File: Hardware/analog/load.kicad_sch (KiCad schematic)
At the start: 21 parts, among them J201 Würth 74651194R, J202 Würth 74651194R, Q201 IXTH80N075L2, U202 LM431SC

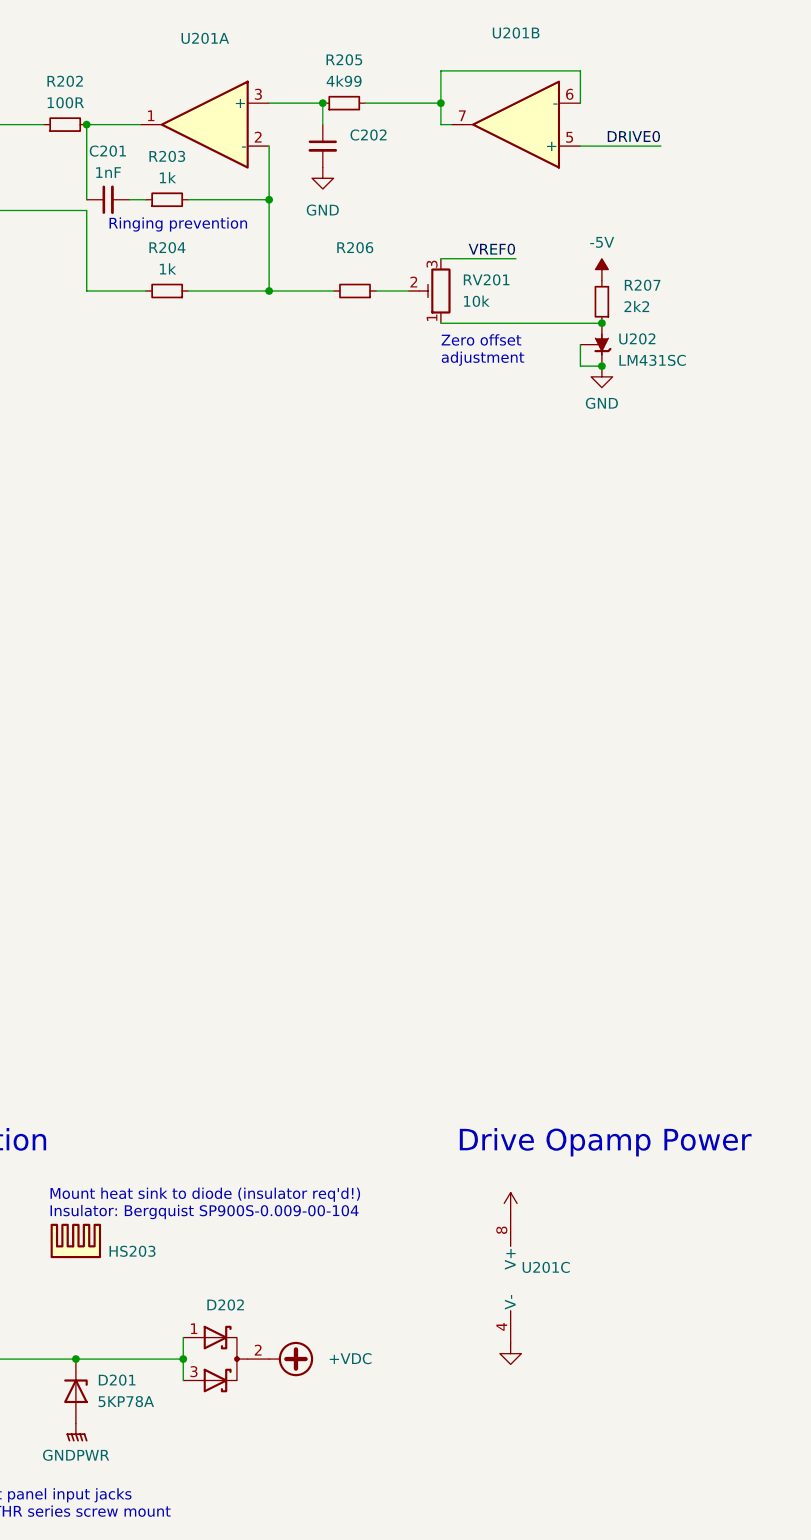
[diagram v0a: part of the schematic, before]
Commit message: Minor analog board layout tweaks
- Mostly to do with the last of the analog bits for the first channel
  (reisstors and capacitors, as well as the zero offset trimmer)
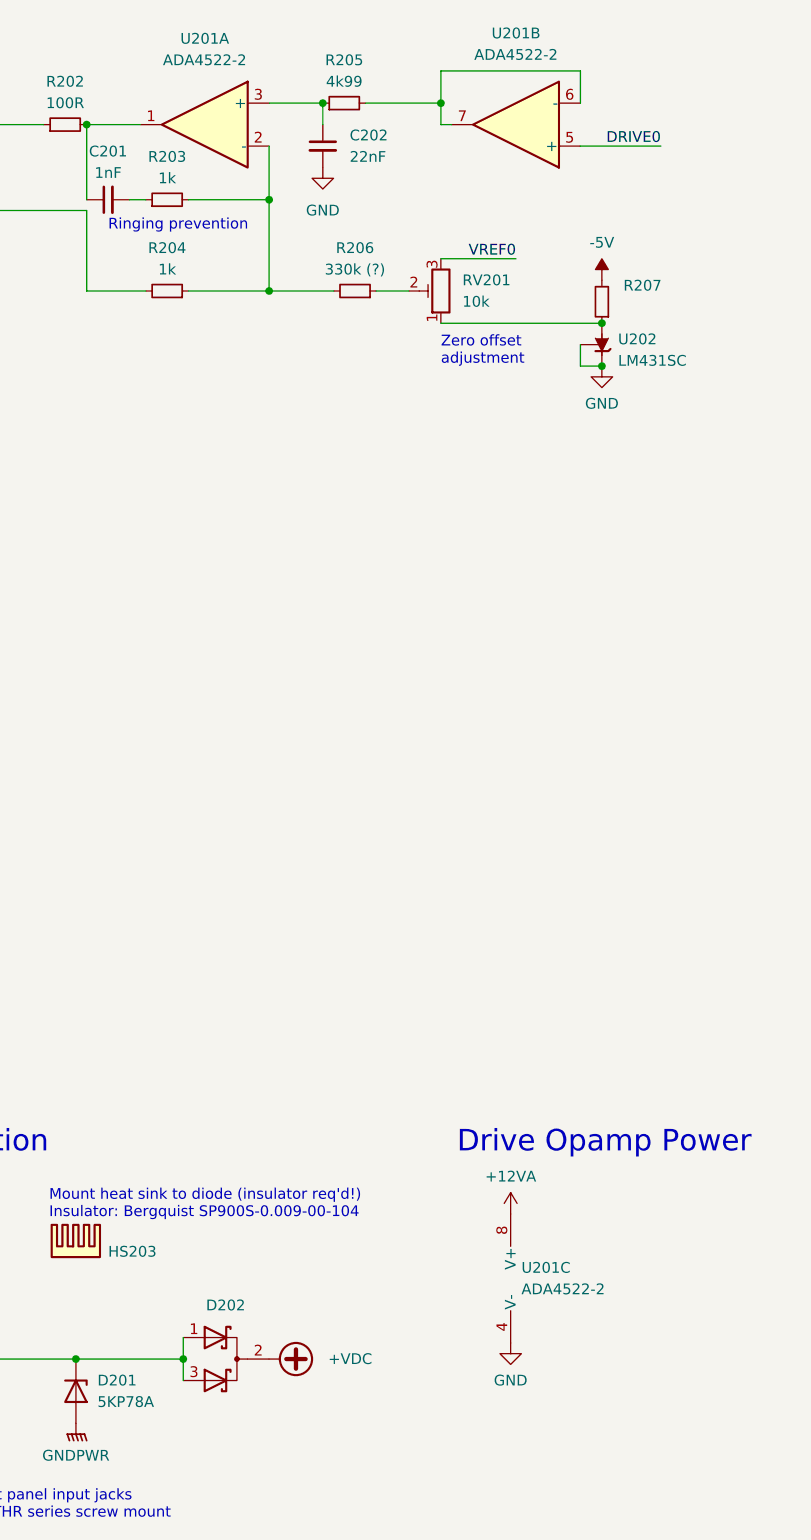
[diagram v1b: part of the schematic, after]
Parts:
- C202: value (none) -> 22nF; footprint (none) -> Capacitor_SMD:C_0805_2012Metric_Pad1.18x1.45mm_HandSolder
- R206: value (none) -> 330k (?)
- R207: value 2k2 -> (none); footprint Resistor_SMD:R_0805_2012Metric_Pad1.20x1.40mm_HandSolder -> (none); MPN RMC1/10-222JTP -> CR0805-JW-102ELF
- U201: value (none) -> ADA4522-2; footprint (none) -> Package_SO:SOIC-8_3.9x4.9mm_P1.27mm
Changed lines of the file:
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@@
       (effects (font (size 1.27 1.27)) (justify left))
     )
-    (property "Value" "" (id 1) (at 82.55 34.2962 0)
-      (effects (font (size 1.27 1.27)) (justify left))
-    )
-    (property "Footprint" "" (id 2) (at 79.375 33.02 0)
+    (property "Value" "22nF" (id 1) (at 82.55 34.2962 0)
+      (effects (font (size 1.27 1.27)) (justify left))
+    )
+    (property "Footprint" "Capacitor_SMD:C_0805_2012Metric_Pad1.18x1.45mm_HandSolder" (id 2) (at 79.375 33.02 0)
       (effects (font (size 1.27 1.27)) hide)
     )
@@
       (effects (font (size 1.27 1.27)) hide)
     )
-    (property "Value" "" (id 1) (at 101.6 154.94 0))
+    (property "Value" "+12VA" (id 1) (at 101.6 154.94 0))
     (property "Footprint" "" (id 2) (at 101.6 159.385 0)
       (effects (font (size 1.27 1.27)) hide)
@@
     (in_bom yes) (on_board yes) (fields_autoplaced)
     (property "Reference" "U201" (id 0) (at 65.405 20.32 0))
-    (property "Value" "" (id 1) (at 65.405 22.86 0))
-    (property "Footprint" "" (id 2) (at 65.405 30.48 0)
+    (property "Value" "ADA4522-2" (id 1) (at 65.405 22.86 0))
+    (property "Footprint" "Package_SO:SOIC-8_3.9x4.9mm_P1.27mm" (id 2) (at 65.405 30.48 0)
       (effects (font (size 1.27 1.27)) hide)
     )
@@
       (effects (font (size 1.27 1.27)) (justify right))
     )
-    (property "Value" "" (id 1) (at 102.87 168.2749 0)
-      (effects (font (size 1.27 1.27)) (justify right))
-    )
-    (property "Footprint" "" (id 2) (at 99.06 167.005 0)
+    (property "Value" "ADA4522-2" (id 1) (at 102.87 168.2749 0)
+      (effects (font (size 1.27 1.27)) (justify right))
+    )
+    (property "Footprint" "Package_SO:SOIC-8_3.9x4.9mm_P1.27mm" (id 2) (at 99.06 167.005 0)
       (effects (font (size 1.27 1.27)) hide)
     )
@@
       (effects (font (size 1.27 1.27)) (justify right))
     )
-    (property "Value" "2k2" (id 1) (at 114.935 52.07 0)
-      (effects (font (size 1.27 1.27)) (justify right))
-    )
-    (property "Footprint" "Resistor_SMD:R_0805_2012Metric_Pad1.20x1.40mm_HandSolder" (id 2) (at 112.395 51.435 0)
+    (property "Value" "" (id 1) (at 114.935 52.07 0)
+      (effects (font (size 1.27 1.27)) (justify right))
+    )
+    (property "Footprint" "" (id 2) (at 112.395 51.435 0)
       (effects (font (size 1.27 1.27)) hide)
     )
@@
       (effects (font (size 1.27 1.27)) hide)
     )
-    (property "MPN" "RMC1/10-222JTP" (id 4) (at 112.395 51.435 0)
+    (property "MPN" "CR0805-JW-102ELF" (id 4) (at 112.395 51.435 0)
       (effects (font (size 1.27 1.27)) hide)
     )
@@
     (in_bom yes) (on_board yes) (fields_autoplaced)
     (property "Reference" "U201" (id 0) (at 102.235 19.685 0))
-    (property "Value" "" (id 1) (at 102.235 22.225 0))
-    (property "Footprint" "" (id 2) (at 102.235 30.48 0)
+    (property "Value" "ADA4522-2" (id 1) (at 102.235 22.225 0))
+    (property "Footprint" "Package_SO:SOIC-8_3.9x4.9mm_P1.27mm" (id 2) (at 102.235 30.48 0)
       (effects (font (size 1.27 1.27)) hide)
     )
@@
       (effects (font (size 1.27 1.27)) hide)
     )
-    (property "Value" "" (id 1) (at 101.6 179.07 0))
+    (property "Value" "GND" (id 1) (at 101.6 179.07 0))
     (property "Footprint" "" (id 2) (at 101.6 174.625 0)
       (effects (font (size 1.27 1.27)) hide)
@@
     (in_bom yes) (on_board yes)
     (property "Reference" "R206" (id 0) (at 83.185 45.085 90))
-    (property "Value" "" (id 1) (at 83.185 47.625 90))
+    (property "Value" "330k (?)" (id 1) (at 83.185 47.625 90))
     (property "Footprint" "Resistor_SMD:R_0805_2012Metric_Pad1.20x1.40mm_HandSolder" (id 2) (at 83.185 50.165 0)
       (effects (font (size 1.27 1.27)) hide)

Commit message: More tweaks to load board
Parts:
- R207: value (none) -> 1k; footprint (none) -> Resistor_SMD:R_0805_2012Metric_Pad1.20x1.40mm_HandSolder
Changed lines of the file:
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@@
   (symbol (lib_id "power:+12VA") (at 101.6 159.385 0) (unit 1)
     (in_bom yes) (on_board yes)
-    (property "Reference" "#PWR?" (id 0) (at 101.6 163.195 0)
+    (property "Reference" "#PWR0208" (id 0) (at 101.6 163.195 0)
       (effects (font (size 1.27 1.27)) hide)
     )
@@
       (effects (font (size 1.27 1.27)) (justify right))
     )
-    (property "Value" "" (id 1) (at 114.935 52.07 0)
-      (effects (font (size 1.27 1.27)) (justify right))
-    )
-    (property "Footprint" "" (id 2) (at 112.395 51.435 0)
+    (property "Value" "1k" (id 1) (at 114.935 52.07 0)
+      (effects (font (size 1.27 1.27)) (justify right))
+    )
+    (property "Footprint" "Resistor_SMD:R_0805_2012Metric_Pad1.20x1.40mm_HandSolder" (id 2) (at 112.395 51.435 0)
       (effects (font (size 1.27 1.27)) hide)
     )
@@
   (symbol (lib_id "power:GND") (at 101.6 174.625 0) (unit 1)
     (in_bom yes) (on_board yes) (fields_autoplaced)
-    (property "Reference" "#PWR?" (id 0) (at 101.6 180.975 0)
-      (effects (font (size 1.27 1.27)) hide)
-    )
+    (property "Reference" "#PWR0209" (id 0) (at 101.6 180.975 0)
+      (effects (font (size 1.27 1.27)) hide)
+    )

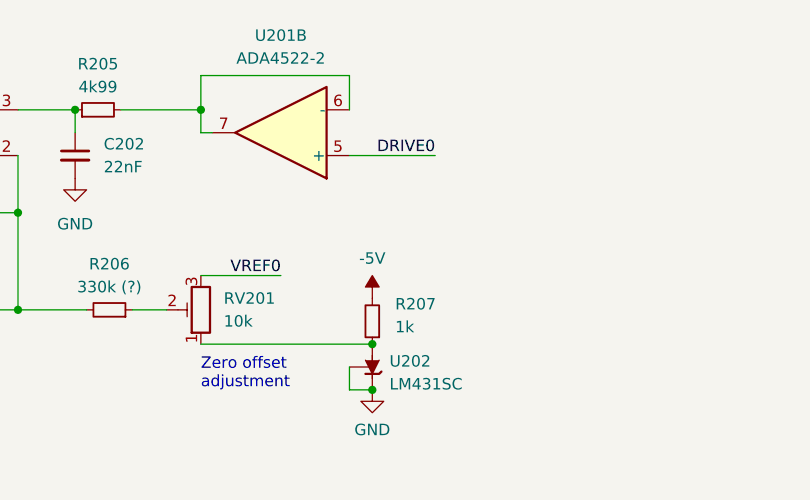
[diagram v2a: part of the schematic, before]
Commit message: Add ADC aliasing filters
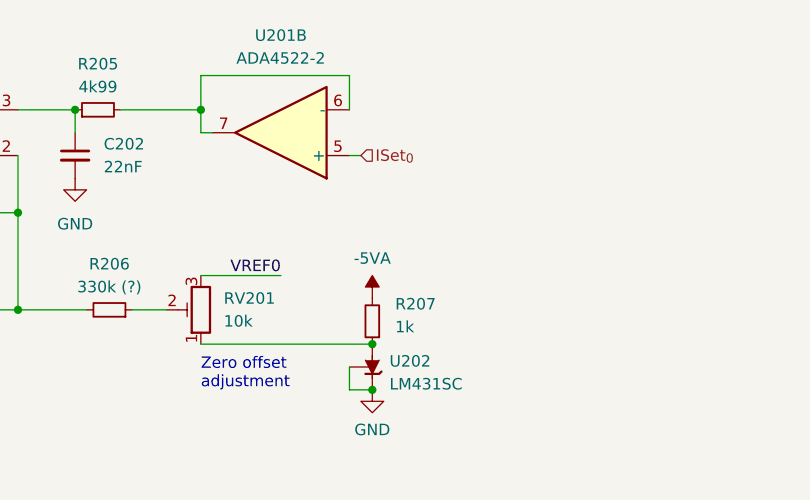
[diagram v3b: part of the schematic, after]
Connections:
- net -5V renamed -5VA
- net DRIVE0 renamed ISet_{0}
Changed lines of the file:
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@@
+    (stroke (width 0) (type default) (color 0 0 0 0))
+  )
+  (wire (pts (xy 109.855 33.02) (xy 111.125 33.02))
     (stroke (width 0) (type default) (color 0 0 0 0))
   )
@@
   )
   (wire (pts (xy 40.005 30.48) (xy 46.355 30.48))
-    (stroke (width 0) (type default) (color 0 0 0 0))
-  )
-  (wire (pts (xy 109.855 33.02) (xy 119.38 33.02))
     (stroke (width 0) (type default) (color 0 0 0 0))
   )
@@
     (effects (font (size 1.27 1.27)) (justify left bottom))
   )
-  (label "DRIVE0" (at 119.38 33.02 180)
-    (effects (font (size 1.27 1.27)) (justify right bottom))
-  )
   (label "VBUS_IN" (at 31.75 176.53 0)
     (effects (font (size 1.27 1.27)) (justify left bottom))
@@
   (label "VREF0" (at 102.235 46.355 180)
     (effects (font (size 1.27 1.27)) (justify right bottom))
+  )
+  (hierarchical_label "ISet_{0}" (shape input) (at 111.125 33.02 0)
+    (effects (font (size 1.27 1.27)) (justify left))
   )
   (symbol (lib_id "Device:R_Small") (at 60.96 39.37 90) (unit 1)
@@
     (pin "8")
   )
-  (symbol (lib_id "power:-5V") (at 112.395 48.895 0) (mirror y) (unit 1)
-    (in_bom yes) (on_board yes)
-    (property "Reference" "#PWR0206" (id 0) (at 112.395 46.355 0)
-      (effects (font (size 1.27 1.27)) hide)
-    )
-    (property "Value" "-5V" (id 1) (at 112.395 44.45 0))
-    (property "Footprint" "" (id 2) (at 112.395 48.895 0)
-      (effects (font (size 1.27 1.27)) hide)
-    )
-    (property "Datasheet" "" (id 3) (at 112.395 48.895 0)
-      (effects (font (size 1.27 1.27)) hide)
-    )
-    (pin "1")
-  )
   (symbol (lib_id "power:+VDC") (at 73.025 176.53 270) (unit 1)
     (in_bom yes) (on_board yes) (fields_autoplaced)
@@
       (effects (font (size 1.27 1.27)) hide)
     )
+    (pin "1")
+  )
+  (symbol (lib_id "power:-5VA") (at 112.395 48.895 0) (unit 1)
+    (in_bom yes) (on_board yes)
+    (property "Reference" "#PWR0118" (id 0) (at 112.395 46.355 0)
+      (effects (font (size 1.27 1.27)) hide)
+    )
+    (property "Value" "-5VA" (id 1) (at 112.395 44.45 0))
+    (property "Footprint" "" (id 2) (at 112.395 48.895 0)
+      (effects (font (size 1.27 1.27)) hide)
+    )
+    (property "Datasheet" "" (id 3) (at 112.395 48.895 0)
+      (effects (font (size 1.27 1.27)) hide)
+    )

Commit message: More tweaks to analog board
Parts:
- removed HS202: 2x C40-058-AE, programmable-load:C40-058-AE-DUAL, symbol Mechanical:Heatsink
- added U203: (no value), Package_TO_SOT_THT:TO-92_Inline_Wide, symbol programmable-load:LMT86LPM
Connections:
- net GND: now also U203.3 (GND)
- new net +3V3: U203.1 (Vdd)
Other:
- note added: "Temp Sensing"
- moved on the sheet: HS201
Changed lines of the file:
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@@
     (stroke (width 0) (type default) (color 0 0 0 0))
+  )
+  (text "Temp Sensing" (at 19.05 123.19 0)
+    (effects (font (size 2.54 2.54)) (justify left bottom))
   )
   (text "Drive Opamp Power" (at 95.25 152.4 0)
@@
     (pin "1")
   )
-  (symbol (lib_id "Mechanical:Heatsink") (at 177.165 156.21 270) (unit 1)
-    (in_bom yes) (on_board yes)
-    (property "Reference" "HS202" (id 0) (at 181.61 154.94 90)
-      (effects (font (size 1.27 1.27)) (justify left))
-    )
-    (property "Value" "2x C40-058-AE" (id 1) (at 181.61 157.48 90)
-      (effects (font (size 1.27 1.27)) (justify left))
-    )
-    (property "Footprint" "programmable-load:C40-058-AE-DUAL" (id 2) (at 177.165 156.5148 0)
-      (effects (font (size 1.27 1.27)) hide)
-    )
-    (property "Datasheet" "~" (id 3) (at 177.165 156.5148 0)
-      (effects (font (size 1.27 1.27)) hide)
-    )
-    (property "MPN" "C40-058-AE" (id 4) (at 177.165 156.21 90)
-      (effects (font (size 1.27 1.27)) hide)
-    )
+  (symbol (lib_id "power:+3V3") (at 33.02 125.73 270) (unit 1)
+    (in_bom yes) (on_board yes)
+    (property "Reference" "#PWR0206" (id 0) (at 29.21 125.73 0)
+      (effects (font (size 1.27 1.27)) hide)
+    )
+    (property "Value" "" (id 1) (at 36.195 125.73 90)
+      (effects (font (size 1.27 1.27)) (justify left))
+    )
+    (property "Footprint" "" (id 2) (at 33.02 125.73 0)
+      (effects (font (size 1.27 1.27)) hide)
+    )
+    (property "Datasheet" "" (id 3) (at 33.02 125.73 0)
+      (effects (font (size 1.27 1.27)) hide)
+    )
+    (pin "1")
   )
   (symbol (lib_id "Connector:Screw_Terminal_01x01") (at 26.67 182.88 180) (unit 1)
@@
     (pin "2")
   )
-  (symbol (lib_id "Mechanical:Heatsink") (at 177.165 148.59 270) (unit 1)
-    (in_bom yes) (on_board yes)
-    (property "Reference" "HS201" (id 0) (at 181.61 147.32 90)
-      (effects (font (size 1.27 1.27)) (justify left))
-    )
-    (property "Value" "2x C40-058-AE" (id 1) (at 181.61 149.86 90)
-      (effects (font (size 1.27 1.27)) (justify left))
-    )
-    (property "Footprint" "programmable-load:C40-058-AE-DUAL" (id 2) (at 177.165 148.8948 0)
-      (effects (font (size 1.27 1.27)) hide)
-    )
-    (property "Datasheet" "~" (id 3) (at 177.165 148.8948 0)
-      (effects (font (size 1.27 1.27)) hide)
-    )
-    (property "MPN" "C40-058-AE" (id 4) (at 177.165 148.59 90)
-      (effects (font (size 1.27 1.27)) hide)
-    )
+  (symbol (lib_id "Mechanical:Heatsink") (at 177.165 154.305 270) (unit 1)
+    (in_bom yes) (on_board yes)
+    (property "Reference" "HS201" (id 0) (at 181.61 153.035 90)
+      (effects (font (size 1.27 1.27)) (justify left))
+    )
+    (property "Value" "2x C40-058-AE" (id 1) (at 181.61 155.575 90)
+      (effects (font (size 1.27 1.27)) (justify left))
+    )
+    (property "Footprint" "programmable-load:C40-058-AE-DUAL" (id 2) (at 177.165 154.6098 0)
+      (effects (font (size 1.27 1.27)) hide)
+    )
+    (property "Datasheet" "~" (id 3) (at 177.165 154.6098 0)
+      (effects (font (size 1.27 1.27)) hide)
+    )
+    (property "MPN" "C40-058-AE" (id 4) (at 177.165 154.305 90)
+      (effects (font (size 1.27 1.27)) hide)
+    )
+  )
+  (symbol (lib_id "power:GND") (at 33.02 140.97 0) (unit 1)
+    (in_bom yes) (on_board yes)
+    (property "Reference" "#PWR0210" (id 0) (at 33.02 147.32 0)
+      (effects (font (size 1.27 1.27)) hide)
+    )
+    (property "Value" "" (id 1) (at 33.02 144.78 0))
+    (property "Footprint" "" (id 2) (at 33.02 140.97 0)
+      (effects (font (size 1.27 1.27)) hide)
+    )
+    (property "Datasheet" "" (id 3) (at 33.02 140.97 0)
+      (effects (font (size 1.27 1.27)) hide)
+    )
+    (pin "1")
   )
   (symbol (lib_id "programmable-load:IXTH80N075L2") (at 34.925 30.48 0) (mirror y) (unit 1)
@@
       (effects (font (size 1.27 1.27)) hide)
     )
+    (pin "1")
+    (pin "2")
+    (pin "3")
+  )
+  (symbol (lib_id "programmable-load:LMT86LPM") (at 33.02 133.35 0) (unit 1)
+    (in_bom yes) (on_board yes) (fields_autoplaced)
+    (property "Reference" "U203" (id 0) (at 24.13 132.0799 0)
+      (effects (font (size 1.27 1.27)) (justify right))
+    )
+    (property "Value" "" (id 1) (at 24.13 134.6199 0)
+      (effects (font (size 1.27 1.27)) (justify right))
+    )
+    (property "Footprint" "Package_TO_SOT_THT:TO-92_Inline_Wide" (id 2) (at 33.02 143.51 0)
+      (effects (font (size 1.27 1.27)) hide)
+    )
+    (property "Datasheet" "http://www.ti.com/lit/ds/symlink/lmt86-q1.pdf" (id 3) (at 33.02 133.35 0)
+      (effects (font (size 1.27 1.27)) hide)
+    )
